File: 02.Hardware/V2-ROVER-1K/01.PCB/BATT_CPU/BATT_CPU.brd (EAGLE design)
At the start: 20.8 x 34.8 mm, 70 parts, among them K2 FLEX12, Q1 BSS84W-7-F, Q2 BSS84W-7-F, Q3 2N7002PW, Q4 2N7002PW, Q5 BSS84W-7-F, U1 ATSAMD21G18_QFN, U3 TPS78230DDCR, U6 MAX9062EUK+T, U8 SN74LVC1G19DBVR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

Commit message: Revision antes de enviar a SETI
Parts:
- moved C22 0.10 mm to (11.7, 30.3)
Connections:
- new net VCC_OLED: C21.1, C5.1, U$30.VCC
- net VCC: no longer C21.1, C5.1, U$30.VCC
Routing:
- net VCC: track 52.8 -> 39.6 mm
- net VCC_OLED: track 0.00 -> 4.17 mm
- net GND: track 100.1 -> 102.7 mm, vias 12 -> 24
- net N$1: track 15.2 -> 14.2 mm
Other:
- board text added: "!RESET"
- board text added: "BATT_CPU-v1 rover1k Nov'22"
- board text added: "GND"
- board text added: "SWCLK"
- board text added: "SWDIO"
- board text added: "VCC"

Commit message: Actualizacion CPU y PROG_BATT
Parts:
- added VBUS5, VBUS6: TESTPAD_TPSQB1,27, BeagleBone_Blue_R3:TESTPAD_B1,27
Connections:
- net TXO: now also VBUS6.TP
- net VBUS: now also VBUS5.TP
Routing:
- net TXO: track 30.7 -> 40.4 mm
- net VBUS: track 74.7 -> 77.4 mm
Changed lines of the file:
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@@
 <layers>
 <layer number="1" name="Top" color="4" fill="1" visible="yes" active="yes"/>
-<layer number="2" name="Route2" color="11" fill="1" visible="yes" active="yes"/>
+<layer number="2" name="Route2" color="11" fill="1" visible="no" active="yes"/>
 <layer number="3" name="Route3" color="4" fill="3" visible="no" active="no"/>
 <layer number="4" name="Route4" color="1" fill="4" visible="no" active="no"/>
@@
 <layer number="13" name="Route13" color="4" fill="5" visible="no" active="no"/>
 <layer number="14" name="Route14" color="1" fill="6" visible="no" active="no"/>
-<layer number="15" name="GND" color="13" fill="1" visible="yes" active="yes"/>
-<layer number="16" name="Bottom" color="1" fill="1" visible="yes" active="yes"/>
+<layer number="15" name="GND" color="13" fill="1" visible="no" active="yes"/>
+<layer number="16" name="Bottom" color="1" fill="1" visible="no" active="yes"/>
 <layer number="17" name="Pads" color="2" fill="1" visible="yes" active="yes"/>
 <layer number="18" name="Vias" color="2" fill="1" visible="yes" active="yes"/>
 <layer number="19" name="Unrouted" color="6" fill="1" visible="yes" active="yes"/>
 <layer number="20" name="Dimension" color="15" fill="1" visible="yes" active="yes"/>
-<layer number="21" name="tPlace" color="14" fill="1" visible="no" active="yes"/>
-<layer number="22" name="bPlace" color="13" fill="1" visible="yes" active="yes"/>
-<layer number="23" name="tOrigins" color="14" fill="1" visible="no" active="yes"/>
-<layer number="24" name="bOrigins" color="13" fill="1" visible="yes" active="yes"/>
-<layer number="25" name="tNames" color="7" fill="1" visible="no" active="yes"/>
-<layer number="26" name="bNames" color="7" fill="1" visible="yes" active="yes"/>
+<layer number="21" name="tPlace" color="14" fill="1" visible="yes" active="yes"/>
+<layer number="22" name="bPlace" color="13" fill="1" visible="no" active="yes"/>
+<layer number="23" name="tOrigins" color="14" fill="1" visible="yes" active="yes"/>
+<layer number="24" name="bOrigins" color="13" fill="1" visible="no" active="yes"/>
+<layer number="25" name="tNames" color="7" fill="1" visible="yes" active="yes"/>
+<layer number="26" name="bNames" color="7" fill="1" visible="no" active="yes"/>
 <layer number="27" name="tValues" color="7" fill="1" visible="no" active="yes"/>
 <layer number="28" name="bValues" color="7" fill="1" visible="no" active="yes"/>
@@
 <layer number="37" name="tTest" color="7" fill="1" visible="no" active="yes"/>
 <layer number="38" name="bTest" color="7" fill="1" visible="no" active="yes"/>
-<layer number="39" name="tKeepout" color="4" fill="11" visible="no" active="yes"/>
-<layer number="40" name="bKeepout" color="1" fill="11" visible="yes" active="yes"/>
-<layer number="41" name="tRestrict" color="4" fill="10" visible="no" active="yes"/>
-<layer number="42" name="bRestrict" color="1" fill="10" visible="yes" active="yes"/>
+<layer number="39" name="tKeepout" color="4" fill="11" visible="yes" active="yes"/>
+<layer number="40" name="bKeepout" color="1" fill="11" visible="no" active="yes"/>
+<layer number="41" name="tRestrict" color="4" fill="10" visible="yes" active="yes"/>
+<layer number="42" name="bRestrict" color="1" fill="10" visible="no" active="yes"/>
 <layer number="43" name="vRestrict" color="2" fill="10" visible="no" active="yes"/>
 <layer number="44" name="Drills" color="7" fill="1" visible="no" active="yes"/>
@@
 <layer number="49" name="Reference" color="7" fill="1" visible="no" active="yes"/>
 <layer number="50" name="dxf" color="7" fill="1" visible="no" active="yes"/>
-<layer number="51" name="tDocu" color="7" fill="1" visible="no" active="yes"/>
-<layer number="52" name="bDocu" color="7" fill="1" visible="yes" active="yes"/>
+<layer number="51" name="tDocu" color="7" fill="1" visible="yes" active="yes"/>
+<layer number="52" name="bDocu" color="7" fill="1" visible="no" active="yes"/>
 <layer number="53" name="tGND_GNDA" color="7" fill="9" visible="no" active="no"/>
 <layer number="54" name="bGND_GNDA" color="1" fill="9" visible="no" active="no"/>
@@
 <attribute name="VALUE" value="0.1uF" x="20.48" y="13.87" size="1.27" layer="27" rot="R90"/>
 </element>
+<element name="VBUS5" library="BeagleBone_Blue_R3" package="TESTPAD_B1,27" value="TESTPAD_TPSQB1,27" x="17.26" y="20.84" smashed="yes">
+<attribute name="NAME" x="16.625" y="21.856" size="1.27" layer="25" ratio="10"/>
+<attribute name="TP_SIGNAL_NAME" value="" x="16.625" y="18.935" size="1" layer="37"/>
+<attribute name="VALUE" x="16.625" y="20.078" size="0.0254" layer="27"/>
+</element>
+<element name="VBUS6" library="BeagleBone_Blue_R3" package="TESTPAD_B1,27" value="TESTPAD_TPSQB1,27" x="19.01" y="21.12" smashed="yes">
+<attribute name="NAME" x="23.775" y="18.006" size="1.27" layer="25" ratio="10"/>
+<attribute name="TP_SIGNAL_NAME" value="" x="18.375" y="19.215" size="1" layer="37"/>
+<attribute name="VALUE" x="18.375" y="20.358" size="0.0254" layer="27"/>
+</element>
 </elements>
 <signals>
@@
 <wire x1="6.117" y1="16.557" x2="6.117" y2="16.637" width="0.2032" layer="1"/>
 <wire x1="6.117" y1="16.637" x2="6.287" y2="16.807" width="0.2032" layer="1"/>
+<contactref element="VBUS5" pad="TP"/>
+<wire x1="14.99" y1="21.75" x2="15.9" y2="20.84" width="0.2032" layer="1"/>
+<wire x1="15.9" y1="20.84" x2="17.26" y2="20.84" width="0.2032" layer="1"/>
 </signal>
 <signal name="AREF">
@@
 <wire x1="10.615" y1="6.355" x2="10.615" y2="6.936" width="0.2032" layer="1"/>
 <wire x1="11" y1="5.97" x2="10.615" y2="6.355" width="0.2032" layer="1"/>
+<contactref element="VBUS6" pad="TP"/>
+<wire x1="19.01" y1="21.12" x2="19.92" y2="22.03" width="0.2032" layer="1"/>
+<wire x1="19.92" y1="22.03" x2="20.57" y2="22.03" width="0.2032" layer="1"/>
+<wire x1="20.703" y1="23.0322" x2="20.7" y2="23.0352" width="0.2032" layer="1"/>
+<wire x1="20.57" y1="22.03" x2="20.703" y2="22.163" width="0.2032" layer="1"/>
+<wire x1="20.703" y1="22.163" x2="20.703" y2="23.0322" width="0.2032" layer="1"/>
+<wire x1="19.836" y1="27.554" x2="17.951" y2="27.554" width="0.2032" layer="1"/>
+<wire x1="20.7" y1="23.0352" x2="20.7" y2="26.69" width="0.2032" layer="1"/>
+<wire x1="20.7" y1="26.69" x2="19.836" y2="27.554" width="0.2032" layer="1"/>
 </signal>
 <signal name="VINSENSE">

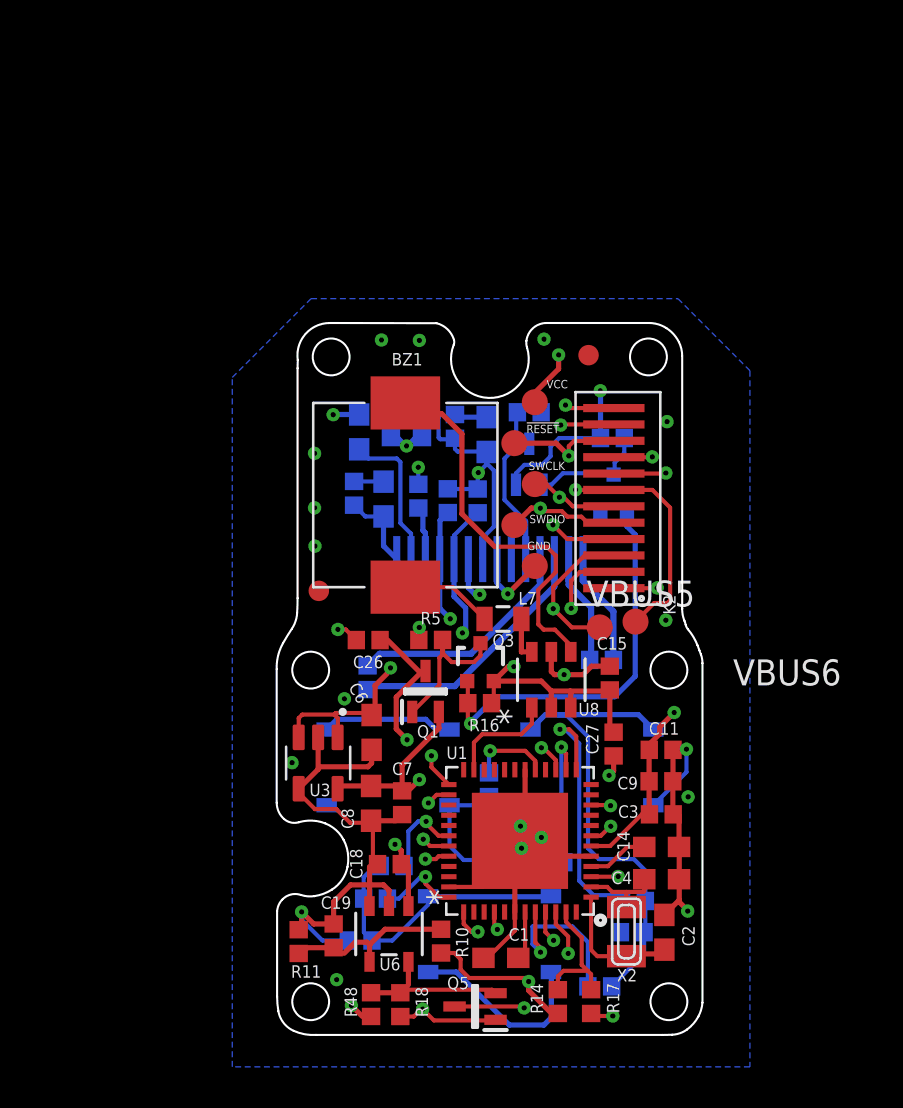
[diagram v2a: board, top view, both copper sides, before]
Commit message: Cambio de faja por conector interPCB. Issue #1
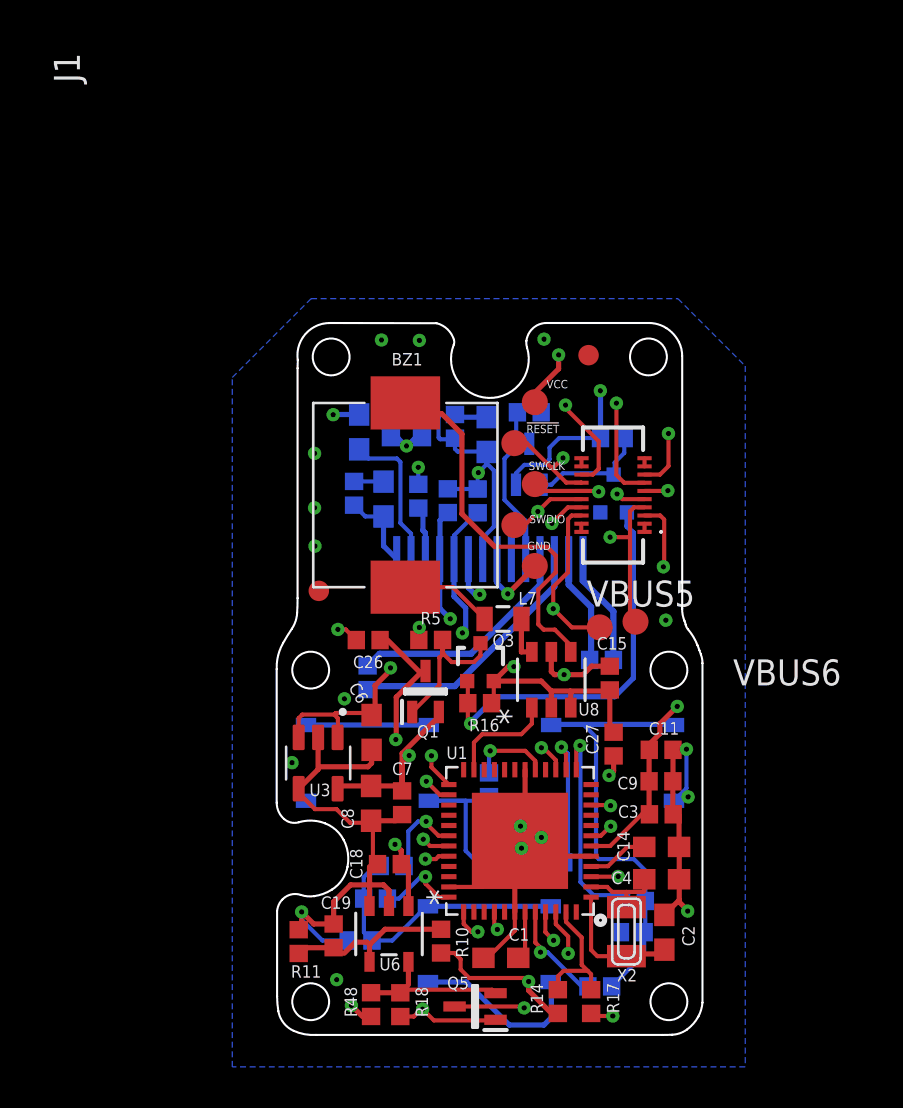
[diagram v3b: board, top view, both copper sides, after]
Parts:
- removed K2: FLEX12, Flex:FLEX6
- added J1: DF40C_2.0_-20DS-0.4V_51_, DF40C_2.0_-20DS-0.4V_51_:DF40C2020DS04V51
- moved S1 1.03 mm to (5.91, 14.2)
- moved S2 1.03 mm to (17.9, 14.2)
- moved S3 0.49 mm to (11.9, 5.36)
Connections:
- new net N$20: J1.1, J1.3
- new net N$21: J1.2, J1.4
- new net N$8: J1.18, J1.20
- new net N$9: J1.17, J1.19
- net !RESET: now also J1.14; no longer K2.10
- net EN_DCDC: now also J1.9; no longer K2.4
- net FB_DAC: now also J1.5; no longer K2.1
- net GND: now also J1.8; no longer K2.2
- net IOSENSE: now also J1.15; no longer K2.8
- net OP_SWITCH: now also J1.13; no longer K2.11
- net SWCLK: now also J1.12; no longer K2.6
- net SWDIO: now also J1.10; no longer K2.5
- net TXO: now also J1.7; no longer K2.7
- net VBUS: now also J1.6; no longer K2.3
- net VCC_2: now also J1.16; no longer K2.12
- net VOUTSENSE: now also J1.11; no longer K2.9
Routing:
- net TXO: track 40.4 -> 31.7 mm
- net GND: track 102.7 -> 99.1 mm, vias 24 -> 23
- net IOSENSE: track 22.1 -> 25.4 mm
- net SWCLK: track 36.9 -> 34.1 mm
- net S_DOWN: track 13.1 -> 10.6 mm
- net VCC: track 39.6 -> 37.2 mm
- net SWDIO: track 36.7 -> 34.2 mm
- net FB_DAC: track 18.3 -> 20.7 mm
- net VCC_2: track 63.0 -> 65.4 mm
- net N$2: track 9.02 -> 11.3 mm
- net N$3: track 25.2 -> 23.3 mm
- net VOUTSENSE: track 20.7 -> 19.0 mm
- net EN_DCDC: track 23.4 -> 22.2 mm
- net !CPU_OP_SWITCH: track 17.3 -> 18.4 mm
- net VBUS: track 77.4 -> 78.2 mm
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
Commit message: Ajustes finales CPU Javi. Pendiente Revision
ISSUES: #11, #12,#10,#9,#8,#7,#4
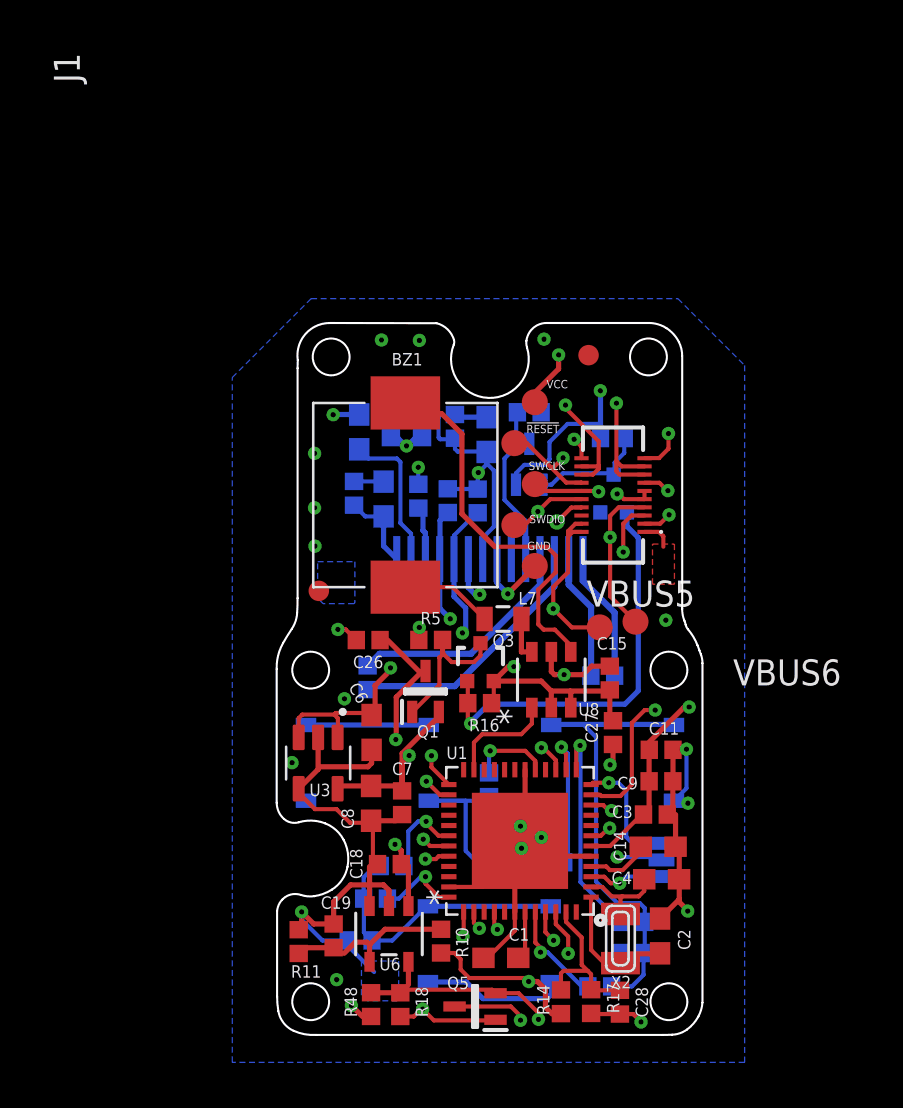
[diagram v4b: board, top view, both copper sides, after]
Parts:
- added C28: 100n, SparkFun-Capacitors:0402
- added JP1: JUMPER-SMT_3_1-NC_PASTE_SILK, SparkFun-Jumpers:SMT-JUMPER_3_1-NC_PASTE_SILK
- moved C16 1.02 mm to (18.8, 4.93)
- moved R13 1.02 mm to (18.9, 6.45)
- moved C12 0.77 mm to (17.4, 18.5)
- moved C27 0.56 mm to (17.9, 15.7)
- moved X2 0.45 mm to (18.3, 5.64)
- moved C3 0.29 mm to (20.0, 11.7)
- moved C2 0.28 mm to (20.2, 5.77)
- moved C14 0.17 mm to (20.1, 10.1)
- moved R14 0.15 mm to (15.4, 2.55)
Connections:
- removed net N$16: Q5.2, R18.1, R48.1, U6.5
- removed net N$21: J1.2, J1.4
- removed net N$8: J1.18, J1.20
- removed net N$9: J1.17, J1.19
- new net DAC: JP1.3, U1.3
- new net LOW_BATT: Q5.2, R18.1, R48.1, U1.11, U6.5
- new net PWM_DAC: JP1.1, U1.12
- net EN_DCDC: now also J1.11
- net FB_DAC: now also J1.3, JP1.2; no longer J1.5, U1.3
- net GND: now also C28.2, J1.20, J1.6
- net IOSENSE: now also J1.19; no longer J1.15
- net N$20: no longer J1.3
- net OP_SWITCH: now also J1.15, J1.17; no longer J1.13
- net RXI: now also J1.5
- net VBUS: now also J1.2, J1.4; no longer J1.6
- net VCC_2: now also J1.18
- net VINSENSE: now also C28.1
- net VOUTSENSE: now also J1.13; no longer J1.11
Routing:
- net LOW_BATT: track 0.00 -> 36.7 mm, vias 0 -> 2
- net RXI: track 0.00 -> 26.5 mm, vias 0 -> 2
- net N$16: track 7.89 -> 0.00 mm
- net PWM_DAC: track 0.00 -> 6.03 mm, vias 0 -> 1
- net DAC: track 0.00 -> 3.71 mm, vias 0 -> 1
- net SWDIO: track 34.2 -> 30.7 mm
- net GND: track 99.1 -> 101.8 mm, vias 23 -> 24
- net OP_SWITCH: track 59.3 -> 61.2 mm
- net VBUS: track 78.2 -> 79.9 mm
- net VINSENSE: track 6.52 -> 7.89 mm
- net N$20: track 0.40 -> 1.52 mm
- net IOSENSE: track 25.4 -> 24.5 mm
- net TXO: track 31.7 -> 32.6 mm
- net C2P: track 5.54 -> 6.34 mm
- net C2N: track 5.45 -> 6.16 mm
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- added copper zone on layer 16, net GND1
- added copper zone on layer 1, net N$20
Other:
- board text added: "-"

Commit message: Revision de cambios de Javi
Despues de Integracion de prototipo 1 de SETI
Se generan cambios
Los implementa Javi, los revisa David
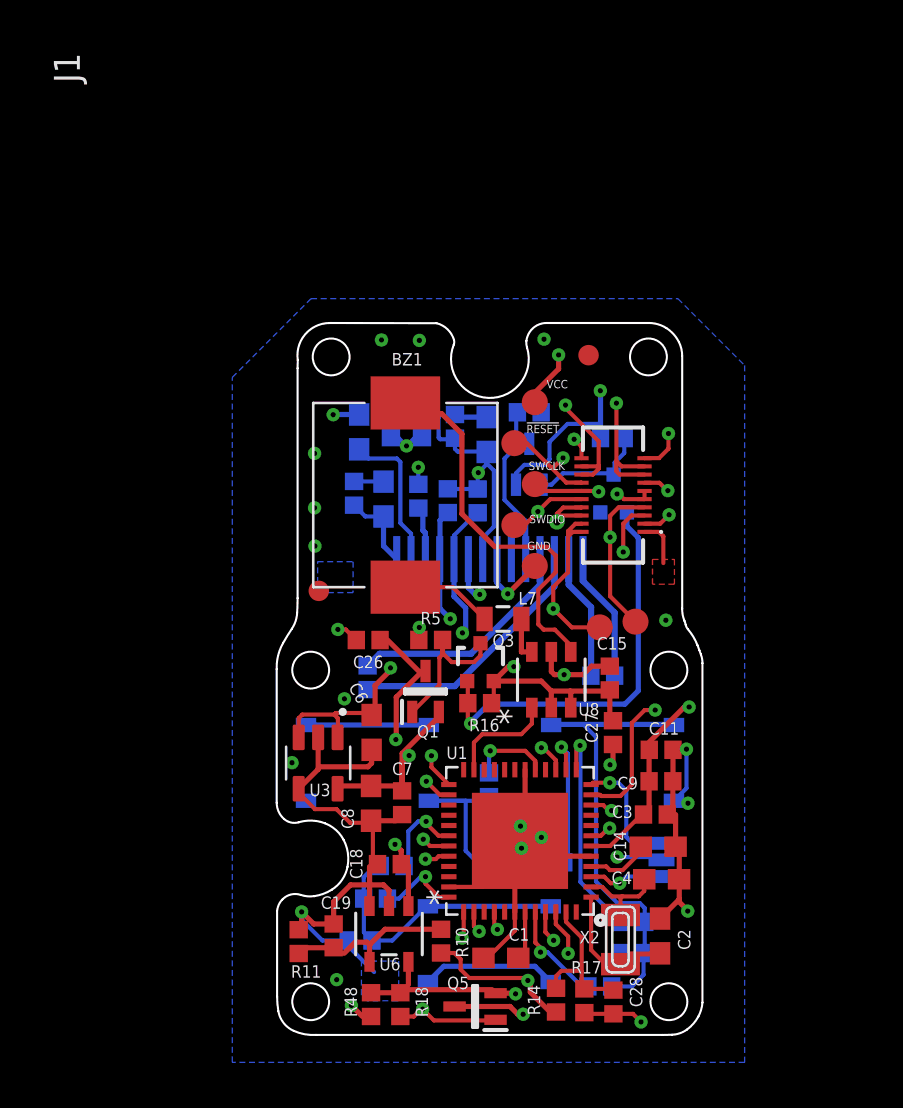
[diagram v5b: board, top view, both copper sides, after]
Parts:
- moved R17 0.33 mm to (16.5, 2.60)
- moved C28 0.32 mm to (17.9, 2.54)
- moved R14 0.25 mm to (15.1, 2.63)
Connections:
- net N$20 renamed SPARE1
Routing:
- net GND: track 101.8 -> 103.6 mm
- net LOW_BATT: track 36.7 -> 35.5 mm
- net SPARE1: track 1.52 -> 2.32 mm
- net OP_SWITCH: track 61.2 -> 60.6 mm
- net VBUS: track 79.9 -> 79.3 mm
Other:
- board text added: "BATT_CPU-v2 rover1k Dec'22"
- board text removed: "BATT_CPU-v1 rover1k Nov'22"

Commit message: Version 2 PCB_CPU y Version 3 BOM_CPU
Cambios menores en el lettering del PCB.

Cambios en la BOM para adecuarse a la  version 2 de la CPU.
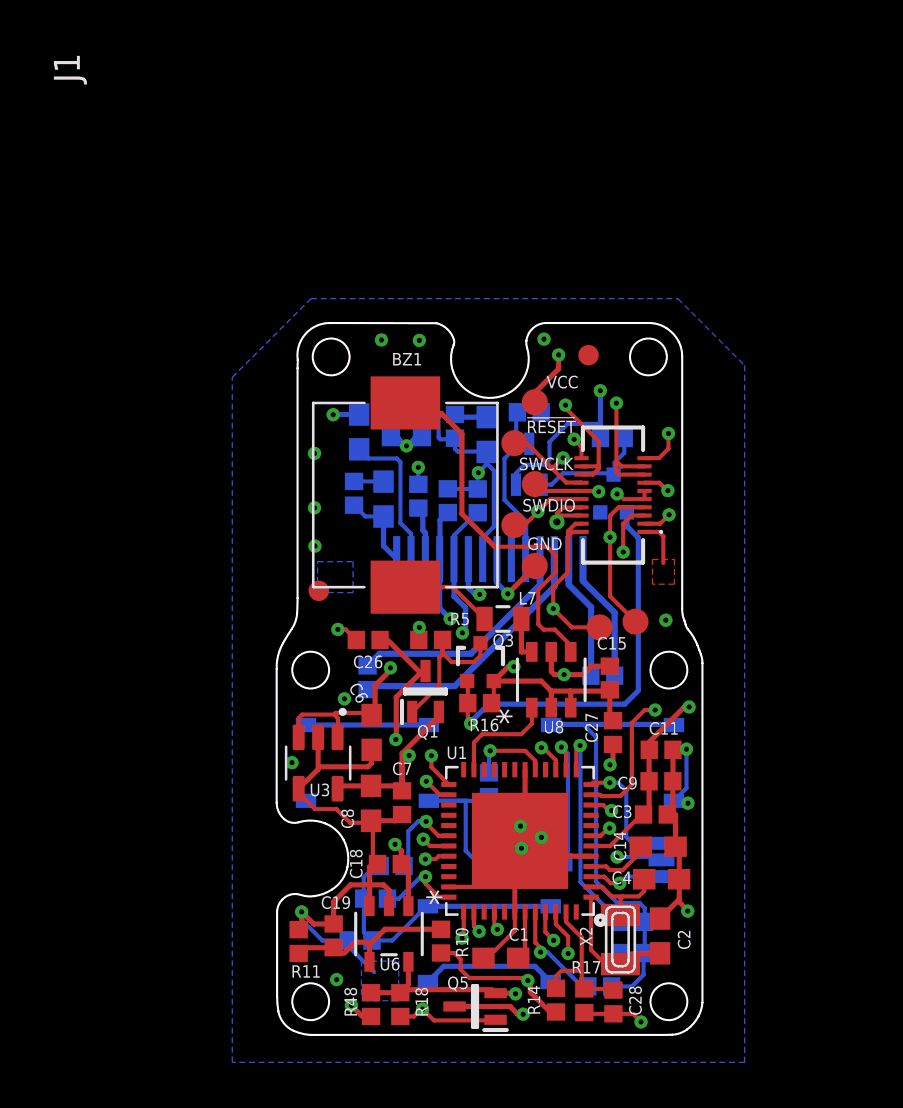
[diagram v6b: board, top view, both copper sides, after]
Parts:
- C18, C26: value 100nF -> 100n
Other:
- board text added: "BATT_CPU rover1k Dec'22-V2"
- board text removed: "BATT_CPU-v2 rover1k Dec'22"
